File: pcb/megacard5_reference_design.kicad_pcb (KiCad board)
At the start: 4 copper layers, 70 x 100 mm, 33 parts, among them J1 MegaCard 5, J11 5V, J12 3V3, J14 GND, J15 VCC, J17 GND, J18 GND, J2 Barrel_Jack_Switch, J3 RJ-064-1, J4 RJ-064-1, J5 RJ-064-1, J6 RJ-064-1, J7 RJ-064-1, J8 ~{EXT_RESET}, J9 ~{POWER_OFF}, SW1 POWER_OFF, SW2 RESET

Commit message: wip
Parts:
- removed J11: 5V, MegaCard5_footprints:5005
- removed J12: 3V3, MegaCard5_footprints:5005
- removed J14, J17, J18: GND, MegaCard5_footprints:5006
- removed J15: VCC, MegaCard5_footprints:5005
- removed J8: ~{EXT_RESET}, MegaCard5_footprints:5007
- removed R6: 4.7k, Resistor_SMD:R_1206_3216Metric
- added J10: SMTSO2545CTJ, MegaCard5_footprints:SMTSO2545CTJ, F.Cu at (72.7, 36.6)
- added J13: SMTSO2545CTJ, MegaCard5_footprints:SMTSO2545CTJ, F.Cu at (96.9, 36.6)
- added SW3: AFT, MegaCard5_footprints:SKRPACE010, F.Cu at (64.0, 58.0)
- added TP1: ~{POWER_OFF}, MegaCard5_footprints:5019, F.Cu at (64.0, 83.6)
- added TP2: VCC, MegaCard5_footprints:5019, F.Cu at (69.7, 93.1)
- added TP3: 5V, MegaCard5_footprints:5019, F.Cu at (81.6, 109.0)
- added TP4: 3V3, MegaCard5_footprints:5019, F.Cu at (81.6, 101.0)
- added TP5: GND, MegaCard5_footprints:5019, F.Cu at (88.9, 105.0)
- added TP6: GND, MegaCard5_footprints:5019, F.Cu at (63.0, 119.6)
- added TP7: GND, MegaCard5_footprints:5019, F.Cu at (69.7, 99.0)
- added TP9: ~{EXT_RESET}, MegaCard5_footprints:5019, F.Cu at (64.0, 89.6)
- C1, C2, C3, C4, C5, R1, R2, R3, R4, R5: moved to F.Cu
- J2: value Barrel_Jack_Switch -> 7V to 50V input; footprint Connector_BarrelJack:BarrelJack_Horizontal -> MegaCard5_footprints:DC-005-5A-2.0-SMT
- J3, J4, J5, J6, J7: value RJ-064-1 -> MJ88-B211-JRS3; footprint MegaCard5_footprints:RJ-064-1 -> MegaCard5_footprints:MJ88-B211-JRS3
- J9: value ~{POWER_OFF} -> X2016WRS-16-9TSW; footprint MegaCard5_footprints:5007 -> MegaCard5_footprints:X2016WRS-16-9TSW
- SW1: value POWER_OFF -> ~{POWER_OFF}; footprint MegaCard5_footprints:SW_PUSH_6mm_H5mm -> MegaCard5_footprints:SKRPACE010
- SW2: value RESET -> ~{EXT_RESET}; footprint MegaCard5_footprints:SW_PUSH_6mm_H5mm -> MegaCard5_footprints:SKRPACE010
- moved J9 27.4 mm to (85.0, 125.0)
- moved SW2 25.8 mm to (64.0, 77.0), turned to 180 degrees
- moved SW1 24.5 mm to (64.0, 69.0), turned to 180 degrees
- moved C1 22.9 mm to (120.8, 107.8)
- moved C2 22.5 mm to (120.8, 89.2)
- moved H2 22.5 mm to (104.5, 33.0), turned to 180 degrees
- moved C3 22.2 mm to (120.8, 70.8)
- moved C5 21.8 mm to (120.8, 52.2)
- moved C4 21.4 mm to (120.8, 33.8)
- moved H3 20.0 mm to (107.0, 126.5)
- moved F1 16.8 mm to (74.2, 94.0), turned to 90 degrees
- moved R1 16.1 mm to (113.5, 107.8)
- moved R2 15.7 mm to (113.5, 89.2)
- moved R3 15.2 mm to (113.5, 70.8)
- moved R5 14.8 mm to (113.5, 52.2)
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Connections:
- F1 pad 1: /VIN -> VIN
- J1 pad 10: unconnected-(J1-RESERVED-Pad10) -> /AFT
- J1 pad 12: unconnected-(J1-SCL/MDC-Pad12) -> /SCL/MDC
- J1 pad 14: unconnected-(J1-SDA/MDIO-Pad14) -> /SDA/MDIO
- J1 pad 17: unconnected-(J1-RESERVED-Pad17) -> /DBG_SWDIO
- J1 pad 18: unconnected-(J1-RESERVED-Pad18) -> /GPIO0
- J1 pad 19: unconnected-(J1-RESERVED-Pad19) -> /DBG_SWCLK
- J1 pad 20: unconnected-(J1-RESERVED-Pad20) -> /GPIO1
- J2 pad 1: /VIN -> VIN
- J9 pad 1: /~{POWER_OFF} -> VIN
- SW1 pad 1: Net-(R6-Pad1) -> GND
- SW1 pad 2: GND -> /~{POWER_OFF}
- SW2 pad 1: /~{EXT_RESET} -> GND
- SW2 pad 2: GND -> /~{EXT_RESET}
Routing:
- net /AFT: track 0.00 -> 80.2 mm
- net GND: track 0.00 -> 75.8 mm, vias 47 -> 162
- net /~{POWER_OFF}: track 22.7 -> 82.1 mm, vias 1 -> 0
- net +3.3V: track 31.7 -> 79.8 mm, vias 0 -> 2
- net /GPIO1: track 0.00 -> 45.6 mm
- net /SCL/MDC: track 0.00 -> 45.0 mm
- net /SDA/MDIO: track 0.00 -> 44.8 mm
- net /GPIO0: track 0.00 -> 44.8 mm
- net /~{EXT_RESET}: track 40.0 -> 78.3 mm, vias 1 -> 2
- net /DBG_SWCLK: track 0.00 -> 37.8 mm
- net /DBG_SWDIO: track 0.00 -> 37.3 mm
- net VIN: track 0.00 -> 34.4 mm
- net /P0_RX-: track 57.2 -> 86.7 mm
- net /P0_RX+: track 58.6 -> 86.8 mm
- net /P3_RX-: track 55.6 -> 82.5 mm
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- added copper zone on B.Cu, net GND
- added copper zone on F.Cu, net GND
- added copper zone on In1.Cu, net GND
- added copper zone on In2.Cu, net GND
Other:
- outline, holes or cut-outs redrawn

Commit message: PCBs ordered v1.0
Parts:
- added G***: LOGO, MegaCard5_footprints:qr_code_wizeus, B.Cu at (95.0, 72.2)
- added G***: LOGO, MegaCard5_footprints:jlcpcb_UL_multilayer15x6.7mm, B.Cu at (85.0, 36.6)
- moved SW3 3.00 mm to (64.0, 61.0)
- turned H1 to -90 degrees
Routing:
- net +3.3V: track 79.8 -> 77.0 mm
- net /AFT: track 80.2 -> 79.6 mm
- net GND: vias 162 -> 169
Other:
- board text added: "0,0900 mm / 0,0000 mm"
- board text added: "0,3000 mm"
- board text added: "1,6062 mm"
- board text added: "3V3"
- board text added: "4"
- board text added: "5V"
- board text added: "70,0000 mm x 100,0000 mm"
- board text added: "AFT"
- board text added: "BOARD CHARACTERISTICS"
- board text added: "Board Thickness:"
- board text added: "Board overall dimensions:"
- board text added: "Carrier Board for MegaCard 5"
- board text added: "Castellated pads:"
- board text added: "Copper Finish:"
- board text added: "Copper Layer Count:"
- board text added: "Documentation:"
- board text added: "Edge card connectors:"
- board text added: "GND"
- board text added: "GPIO0"
- board text added: "GPIO1"
- board text added: "HAL lead-free"
- board text added: "Impedance Control:"
- board text added: "Min hole diameter:"
- board text added: "Min track/spacing:"
- board text added: "No"
- board text added: "Plated Board Edge:"
- board text added: "Rev. 1.0 - 15.09.2024 Designed by Wilhelm Zeuschner"
- board text added: "Rev. 1.0 - 15.09.2024 Designed by Wilhelm Zeuschner Design files available at: https://github.com/wilhelmzeuschner/megacard5_reference_design"
- board text added: "SCL/MDC"
- board text added: "SDA/MDIO"
- board text added: "SWCLK"
- board text added: "SWDIO"
- board text added: "Serial number:"
- board text added: "VIN"
- board text added: "Yes"
- board text added: "wizeus.de/megacard5_carrier"
- board text added: "~{EXT_RESET}"
- board text added: "~{POWER_OFF}"

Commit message: updated PCB to Rev 1.1
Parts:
- removed J9: X2016WRS-16-9TSW, MegaCard5_footprints:X2016WRS-16-9TSW
- added J11: S7B-PH-SM4-TB(LF)(SN), MegaCard5_footprints:JST_PH_S7B-PH-SM4-TB_1x07-1MP_P2.00mm_Horizontal, F.Cu at (75.8, 124.8)
- added J12: S7B-PH-SM4-TB(LF)(SN), MegaCard5_footprints:JST_PH_S7B-PH-SM4-TB_1x07-1MP_P2.00mm_Horizontal, F.Cu at (94.8, 124.8)
- moved H3 0.50 mm to (107.5, 126.5)
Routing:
- net GND: track 75.8 -> 60.7 mm, vias 169 -> 167
- net /DBG_SWDIO: track 37.3 -> 39.8 mm
- net /SDA/MDIO: track 44.8 -> 47.3 mm
- net /GPIO1: track 45.6 -> 48.2 mm
- net /GPIO0: track 44.8 -> 47.3 mm
- net /DBG_SWCLK: track 37.8 -> 40.3 mm
- net /SCL/MDC: track 45.0 -> 46.8 mm
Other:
- board text added: "Rev. 1.1 - 26.10.2024 Designed by Wilhelm Zeuschner"
- board text removed: "Rev. 1.0 - 15.09.2024 Designed by Wilhelm Zeuschner"

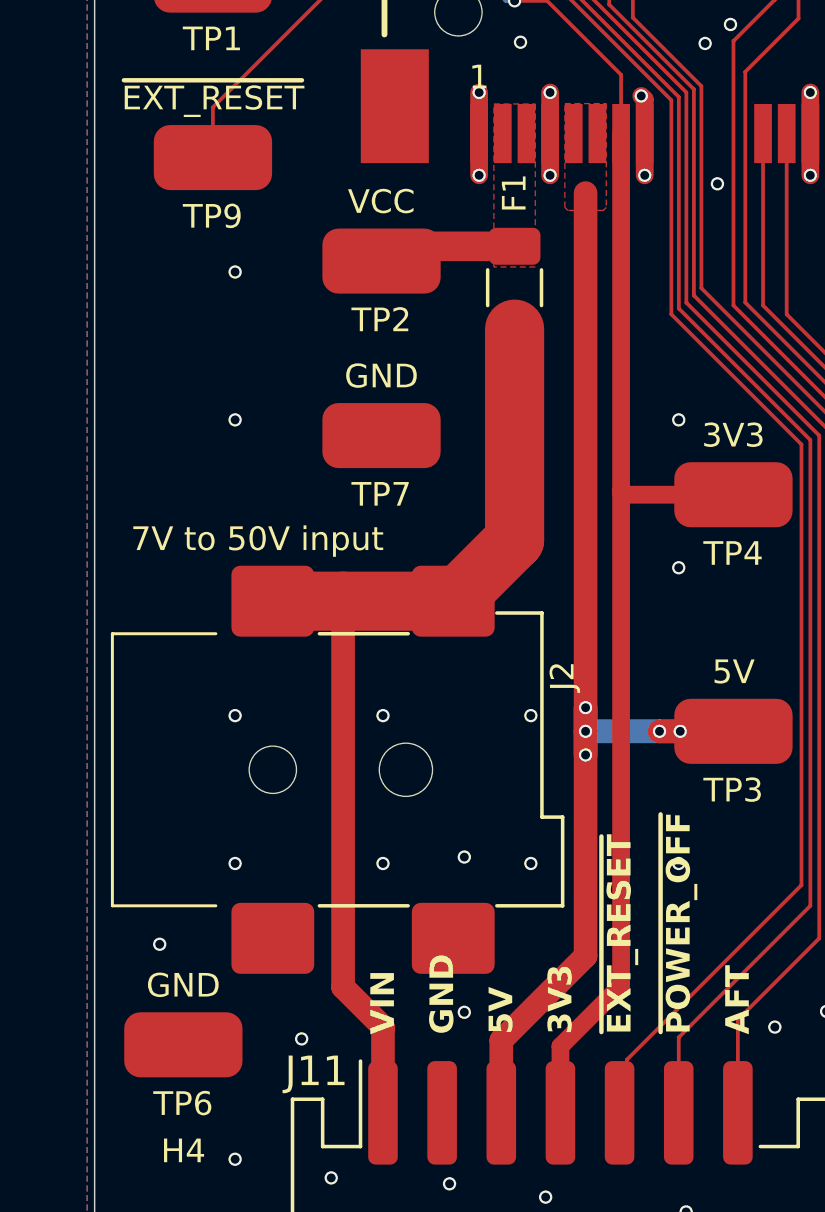
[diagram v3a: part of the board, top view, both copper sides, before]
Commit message: renamed VCC to PWR_IN
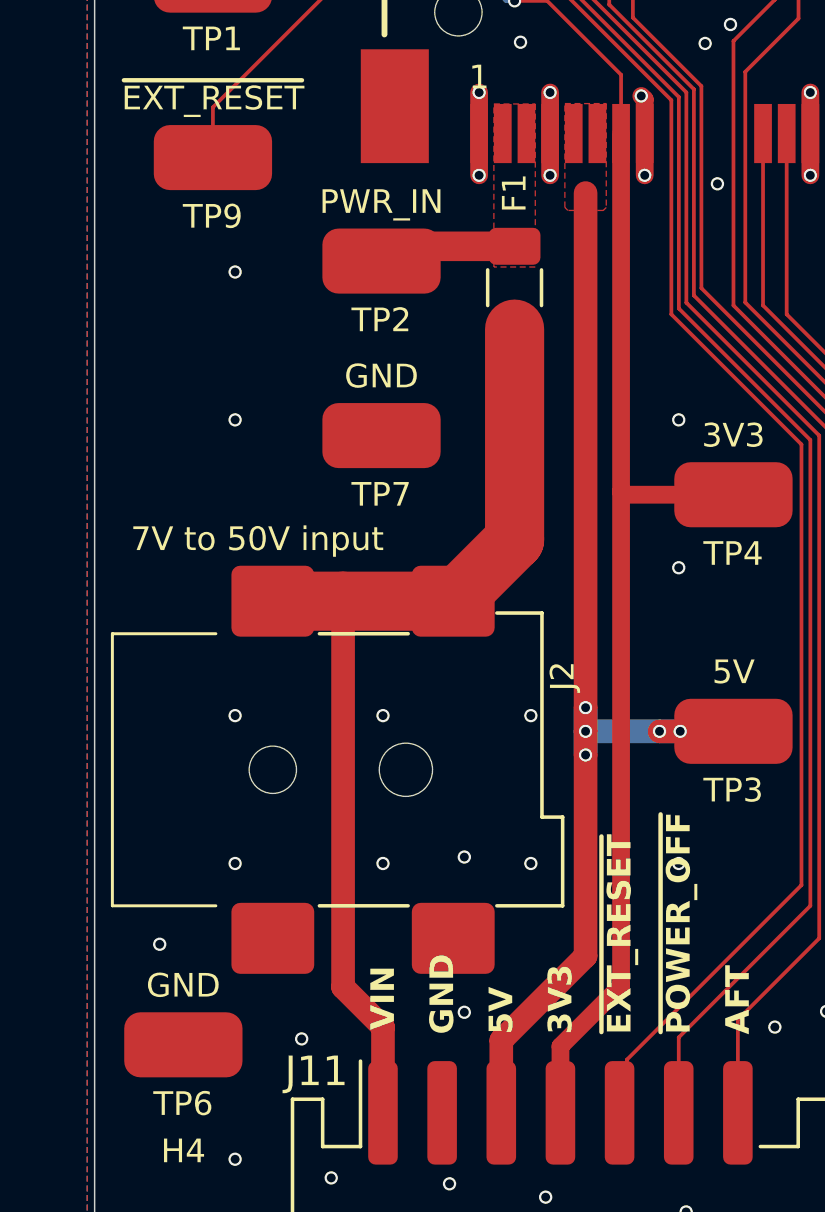
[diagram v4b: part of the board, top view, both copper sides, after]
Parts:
- TP2: value VCC -> PWR_IN
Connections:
- net VCC renamed PWR_IN
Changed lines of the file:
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@@
 	(net 5 "Net-(C4-Pad1)")
 	(net 6 "Net-(C5-Pad1)")
-	(net 7 "VCC")
+	(net 7 "PWR_IN")
 	(net 8 "/~{EXT_RESET}")
 	(net 9 "/P1_RX-")
@@
 			(size 0.6 2)
 			(layers "F.Cu" "F.Paste" "F.Mask")
-			(net 7 "VCC")
+			(net 7 "PWR_IN")
 			(pinfunction "PWR_IN")
 			(pintype "power_in")
@@
 			(size 0.6 2)
 			(layers "F.Cu" "F.Paste" "F.Mask")
-			(net 7 "VCC")
+			(net 7 "PWR_IN")
 			(pinfunction "PWR_IN")
 			(pintype "power_in")
@@
 			(layers "F.Cu" "F.Paste" "F.Mask")
 			(roundrect_rratio 0.2)
-			(net 7 "VCC")
+			(net 7 "PWR_IN")
 			(pintype "passive")
 		)
@@
 			)
 		)
-		(property "Value" "VCC"
+		(property "Value" "PWR_IN"
 			(at 0 2 0)
 			(layer "F.SilkS")
@@
 			(layers "F.Cu" "F.Paste" "F.Mask")
 			(roundrect_rratio 0.25)
-			(net 7 "VCC")
+			(net 7 "PWR_IN")
 			(pinfunction "1")
 			(pintype "passive")
@@
 	)
 	(gr_text "VIN"
-		(at 69.75 119.25 90)
+		(at 69.75 119.1 90)
 		(layer "F.SilkS")
 		(effects
@@
 	(zone
 		(net 7)
-		(net_name "VCC")
+		(net_name "PWR_IN")
 		(layer "F.Cu")
 		(hatch edge 0.5)
